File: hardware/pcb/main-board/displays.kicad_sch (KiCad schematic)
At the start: 1 part, among them J601 DISP_PCB x40 FPC

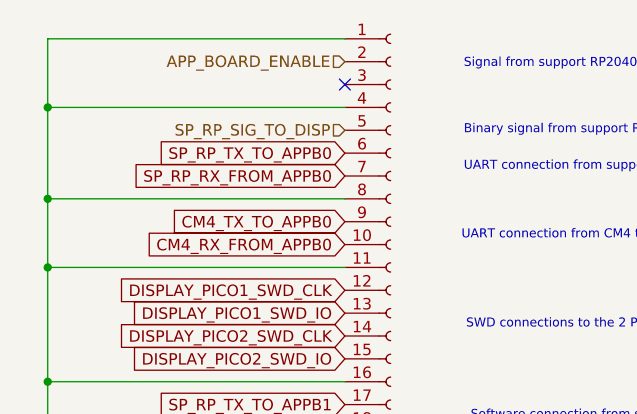
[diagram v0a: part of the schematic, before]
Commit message: more renaming and tidying up of internal interfaces
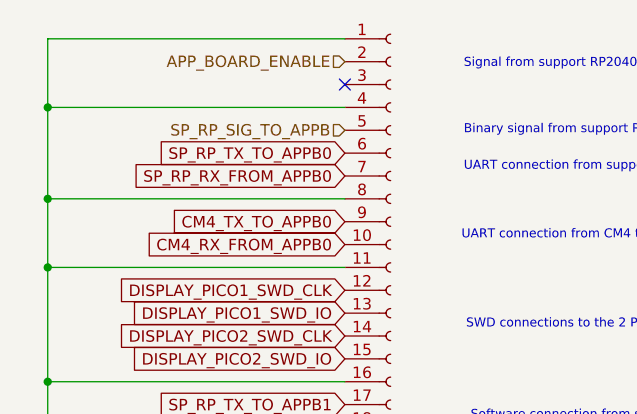
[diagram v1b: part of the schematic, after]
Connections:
- net SP_RP_SIG_TO_DISP renamed SP_RP_SIG_TO_APPB
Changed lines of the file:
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@@
 		)
 	)
-	(hierarchical_label "SP_RP_SIG_TO_DISP"
+	(hierarchical_label "SP_RP_SIG_TO_APPB"
 		(shape input)
 		(at 58.42 33.02 180)

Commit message: tidy the keyboard comms
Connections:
- net KB_TX_TO_APPB0: now reaches J601.19 (Pin_19)
- net KB_RX_FROM_APPB0: now reaches J601.20 (Pin_20)
- net KB_TX_TO_APPB1: now reaches J601.21 (Pin_21)
- net KB_RX_FROM_APPB1: now reaches J601.22 (Pin_22)
- net DISPLAY_PICO1_SWD_CLK renamed APPB_PICO0_SWD_CLK
- net DISPLAY_PICO1_SWD_IO renamed APPB_PICO0_SWD_IO
- net DISPLAY_PICO2_SWD_CLK renamed APPB_PICO1_SWD_CLK
- net DISPLAY_PICO2_SWD_IO renamed APPB_PICO1_SWD_IO
- no-connect marks 15 -> 11
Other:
- note added: "Software connection from keyboard RP to application board Pico1"
- note added: "UART connection from keyboard RP to application board Pico0"
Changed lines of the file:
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@@
-	)
-	(no_connect
-		(at 58.42 68.58)
 	)
 	(no_connect
@@
 	)
 	(no_connect
-		(at 58.42 76.2)
-	)
-	(no_connect
-		(at 58.42 71.12)
-	)
-	(no_connect
 		(at 58.42 101.6)
 	)
@@
 		(at 58.42 99.06)
 	)
-	(no_connect
-		(at 58.42 73.66)
-	)
 	(wire
 		(pts
@@
 		)
 	)
+	(text "Software connection from keyboard RP to application board Pico1"
+		(exclude_from_sim no)
+		(at 72.39 74.93 0)
+		(effects
+			(font
+				(size 1 1)
+			)
+			(justify left)
+		)
+	)
 	(text "Software connection from support RP2040 to application board Pico1"
 		(exclude_from_sim no)
@@
 		)
 	)
+	(text "UART connection from keyboard RP to application board Pico0"
+		(exclude_from_sim no)
+		(at 72.39 69.85 0)
+		(effects
+			(font
+				(size 1 1)
+			)
+			(justify left)
+		)
+	)
 	(text "UART connection from CM4 to application board Pico0"
 		(exclude_from_sim no)
@@
 		)
 	)
-	(global_label "DISPLAY_PICO2_SWD_IO"
+	(global_label "APPB_PICO1_SWD_IO"
 		(shape input)
 		(at 58.42 58.42 180)
@@
 		)
 		(property "Intersheetrefs" "${INTERSHEET_REFS}"
-			(at 34.0756 58.42 0)
+			(at 36.7366 58.42 0)
 			(effects
 				(font
@@
 		)
 	)
-	(global_label "DISPLAY_PICO2_SWD_CLK"
+	(global_label "APPB_PICO1_SWD_CLK"
 		(shape input)
 		(at 58.42 55.88 180)
@@
 		)
 		(property "Intersheetrefs" "${INTERSHEET_REFS}"
-			(at 32.4428 55.88 0)
+			(at 35.1038 55.88 0)
 			(effects
 				(font
@@
 		)
 	)
-	(global_label "DISPLAY_PICO1_SWD_CLK"
+	(global_label "APPB_PICO0_SWD_CLK"
 		(shape input)
 		(at 58.42 50.8 180)
@@
 		)
 		(property "Intersheetrefs" "${INTERSHEET_REFS}"
-			(at 32.4428 50.8 0)
+			(at 35.1038 50.8 0)
 			(effects
 				(font
@@
 		)
 	)
-	(global_label "DISPLAY_PICO1_SWD_IO"
+	(global_label "KB_TX_TO_APPB1"
+		(shape input)
+		(at 58.42 73.66 180)
+		(fields_autoplaced yes)
+		(effects
+			(font
+				(size 1.27 1.27)
+			)
+			(justify right)
+		)
+		(property "Intersheetrefs" "${INTERSHEET_REFS}"
+			(at 40.0629 73.66 0)
+			(effects
+				(font
+					(size 1.27 1.27)
+				)
+				(justify right)
+				(hide yes)
+			)
+		)
+	)
+	(global_label "KB_RX_FROM_APPB0"
+		(shape input)
+		(at 58.42 71.12 180)
+		(fields_autoplaced yes)
+		(effects
+			(font
+				(size 1.27 1.27)
+			)
+			(justify right)
+		)
+		(property "Intersheetrefs" "${INTERSHEET_REFS}"
+			(at 36.9181 71.12 0)
+			(effects
+				(font
+					(size 1.27 1.27)
+				)
+				(justify right)
+				(hide yes)
+			)
+		)
+	)
+	(global_label "KB_TX_TO_APPB0"
+		(shape input)
+		(at 58.42 68.58 180)
+		(fields_autoplaced yes)
+		(effects
+			(font
+				(size 1.27 1.27)
+			)
+			(justify right)
+		)
+		(property "Intersheetrefs" "${INTERSHEET_REFS}"
+			(at 40.0629 68.58 0)
+			(effects
+				(font
+					(size 1.27 1.27)
+				)
+				(justify right)
+				(hide yes)
+			)
+		)
+	)
+	(global_label "APPB_PICO0_SWD_IO"
 		(shape input)
 		(at 58.42 53.34 180)
@@
 		)
 		(property "Intersheetrefs" "${INTERSHEET_REFS}"
-			(at 34.0756 53.34 0)
+			(at 36.7366 53.34 0)
 			(effects
 				(font
@@
 			(effects
 				(font
+					(size 1.27 1.27)
+				)
+				(justify right)
+				(hide yes)
+			)
+		)
+	)
+	(global_label "KB_RX_FROM_APPB1"
+		(shape input)
+		(at 58.42 76.2 180)
+		(fields_autoplaced yes)
+		(effects
+			(font
+				(size 1.27 1.27)
+			)
+			(justify right)
+		)
+		(property "Intersheetrefs" "${INTERSHEET_REFS}"
+			(at 36.9181 76.2 0)
+			(effects
+				(font

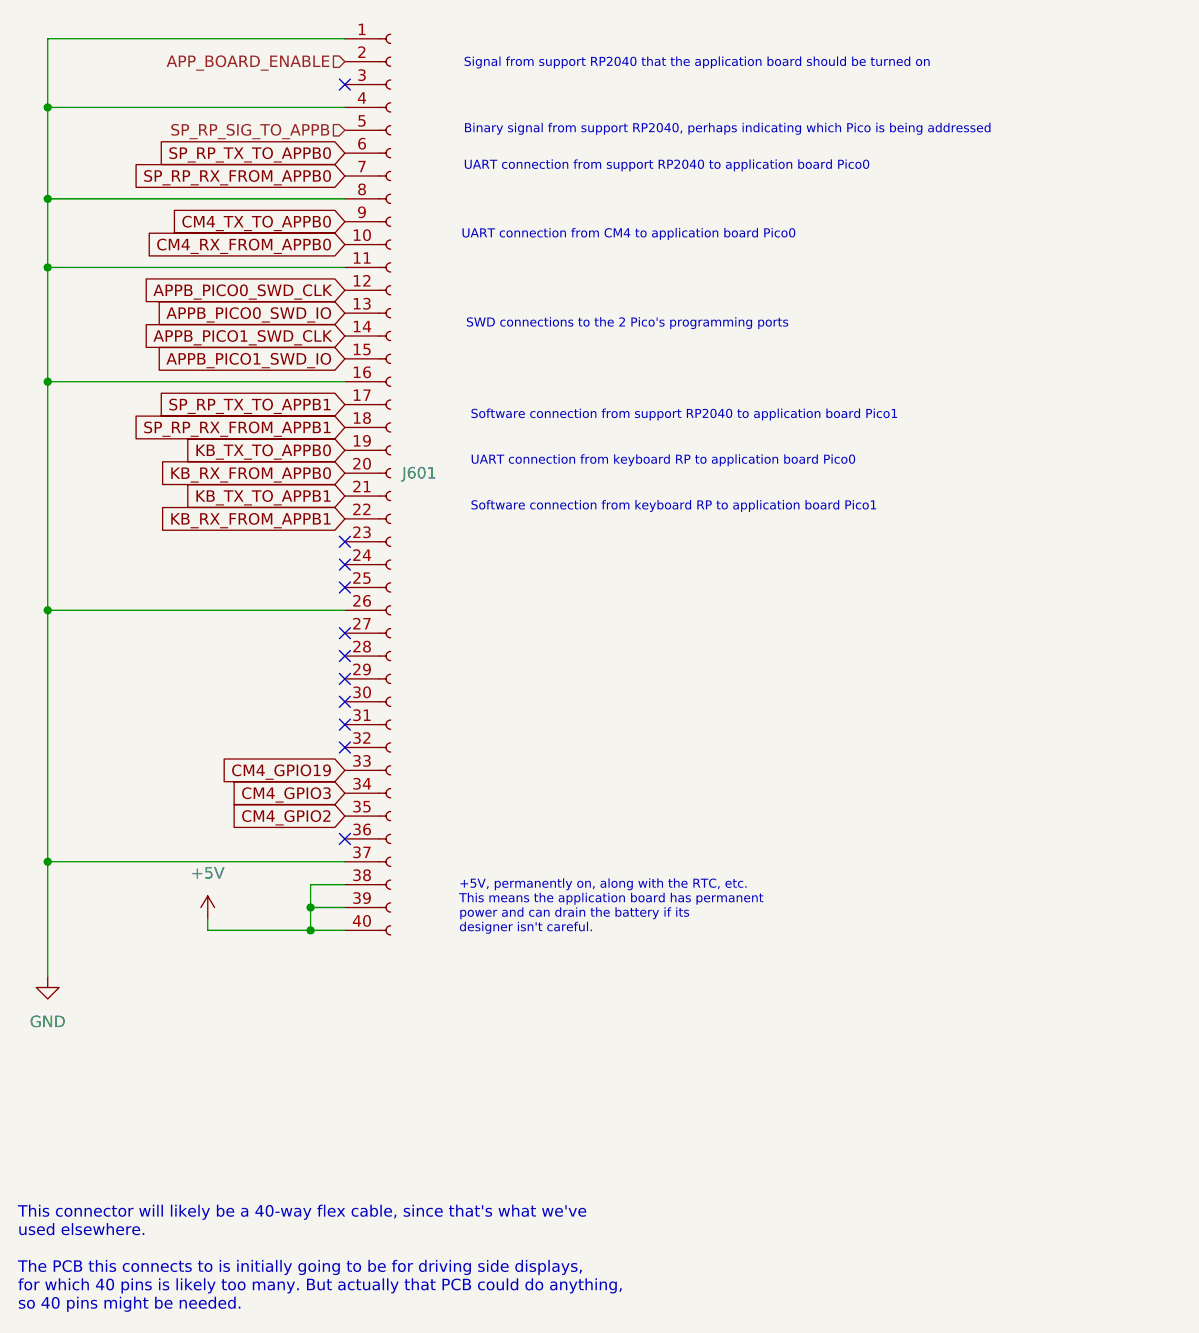
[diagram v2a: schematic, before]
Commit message: rename app board picos to 1 and 2, to match the application board schematics
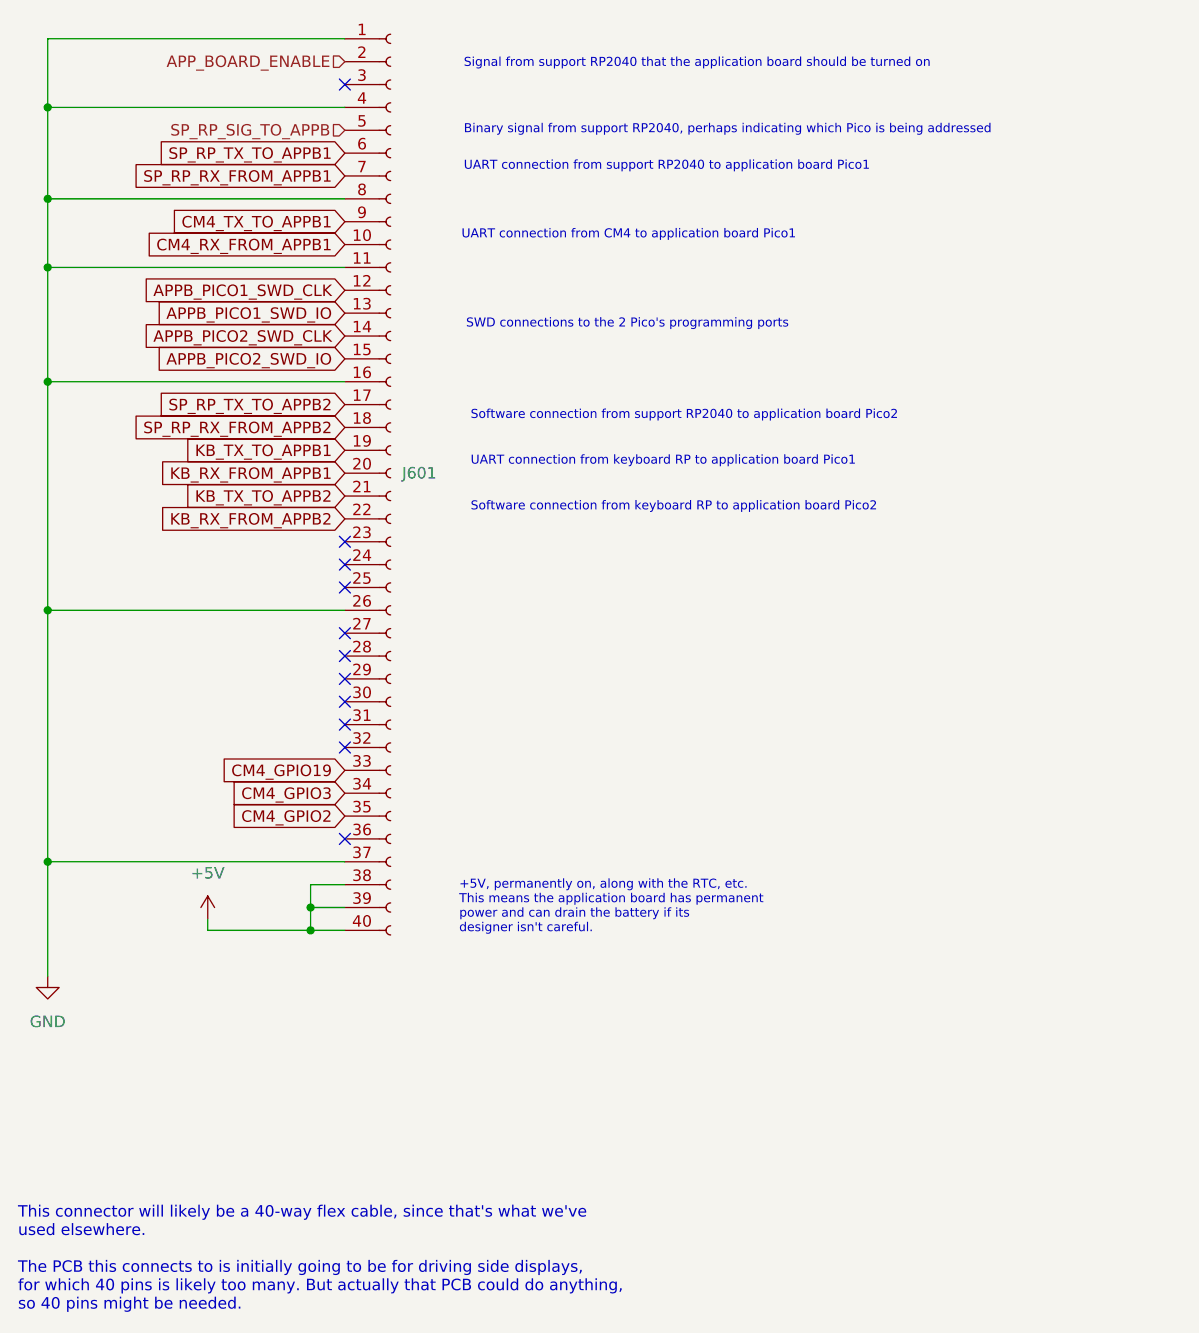
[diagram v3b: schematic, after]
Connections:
- net APPB_PICO0_SWD_CLK is gone; now on net APPB_PICO1_SWD_CLK: J601.12 (Pin_12)
- net APPB_PICO0_SWD_IO is gone; now on net APPB_PICO1_SWD_IO: J601.13 (Pin_13)
- net KB_RX_FROM_APPB0 is gone; now on net KB_RX_FROM_APPB1: J601.20 (Pin_20)
- net KB_TX_TO_APPB0 is gone; now on net KB_TX_TO_APPB1: J601.19 (Pin_19)
- net SP_RP_RX_FROM_APPB0 is gone; now on net SP_RP_RX_FROM_APPB1: J601.7 (Pin_7)
- net SP_RP_TX_TO_APPB0 is gone; now on net SP_RP_TX_TO_APPB1: J601.6 (Pin_6)
- net APPB_PICO1_SWD_CLK: no longer J601.14 (Pin_14)
- net APPB_PICO1_SWD_IO: no longer J601.15 (Pin_15)
- net KB_RX_FROM_APPB1: no longer J601.22 (Pin_22)
- net KB_TX_TO_APPB1: no longer J601.21 (Pin_21)
- net SP_RP_RX_FROM_APPB1: no longer J601.18 (Pin_18)
- net SP_RP_TX_TO_APPB1: no longer J601.17 (Pin_17)
- net CM4_RX_FROM_APPB0 renamed CM4_RX_FROM_APPB1
- net CM4_TX_TO_APPB0 renamed CM4_TX_TO_APPB1
- new net APPB_PICO2_SWD_CLK: J601.14 (Pin_14)
- new net APPB_PICO2_SWD_IO: J601.15 (Pin_15)
- new net KB_RX_FROM_APPB2: J601.22 (Pin_22)
- new net KB_TX_TO_APPB2: J601.21 (Pin_21)
- new net SP_RP_RX_FROM_APPB2: J601.18 (Pin_18)
- new net SP_RP_TX_TO_APPB2: J601.17 (Pin_17)
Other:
- note added: "Software connection from keyboard RP to application board Pico2"
- note added: "Software connection from support RP2040 to application board Pico2"
- note added: "UART connection from CM4 to application board Pico1"
- note added: "UART connection from keyboard RP to application board Pico1"
- note added: "UART connection from support RP2040 to application board Pico1"
- note removed: "Software connection from keyboard RP to application board Pico1"
- note removed: "Software connection from support RP2040 to application board Pico1"
- note removed: "UART connection from CM4 to application board Pico0"
- note removed: "UART connection from keyboard RP to application board Pico0"
- note removed: "UART connection from support RP2040 to application board Pico0"

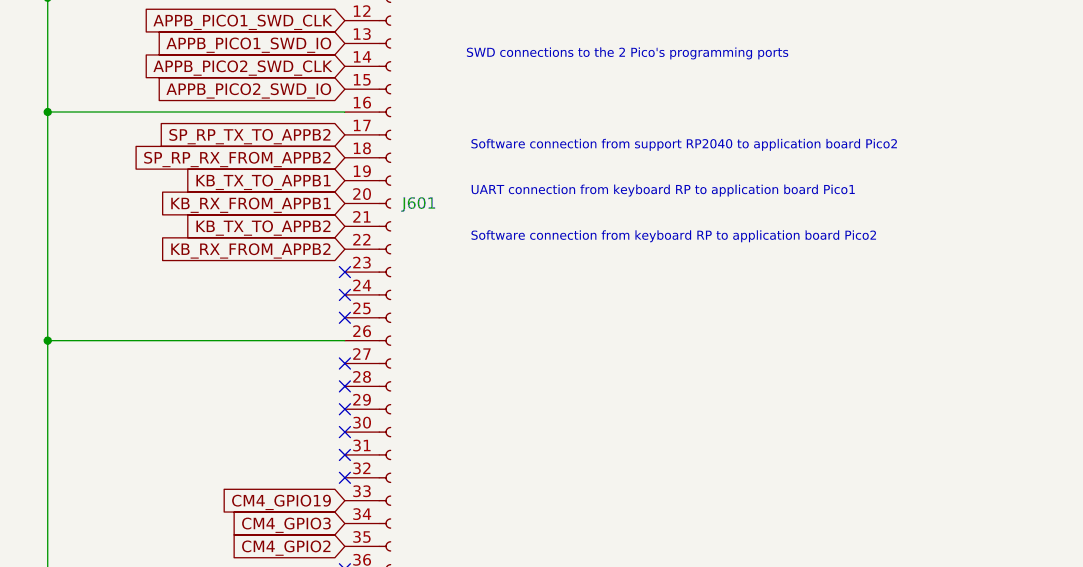
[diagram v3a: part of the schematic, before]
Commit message: move an SWD GPIO freeing up UART4 on the CM4. use that for talking to the appb Pico2
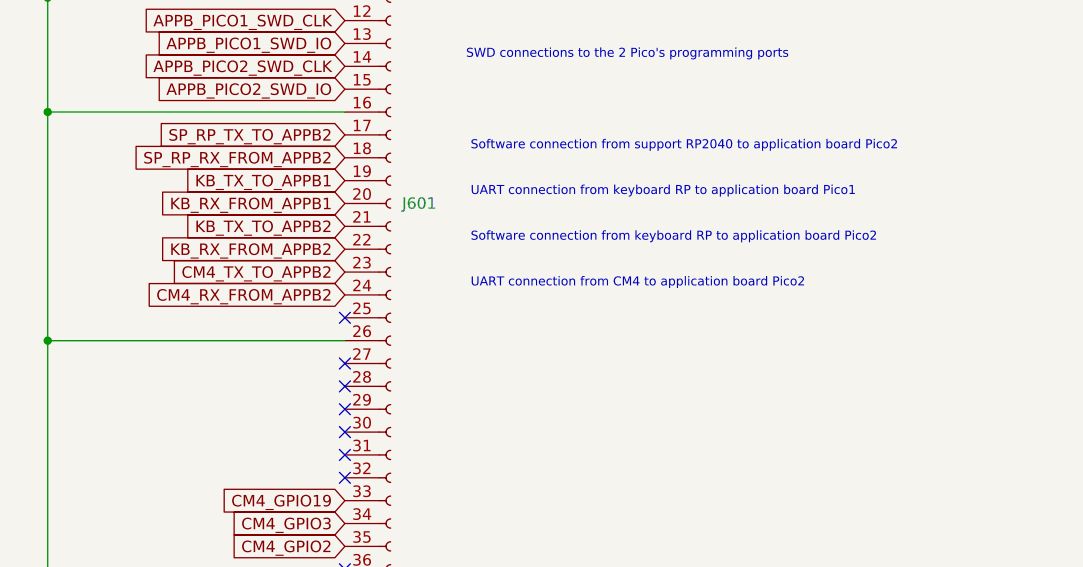
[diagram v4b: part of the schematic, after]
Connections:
- net CM4_TX_TO_APPB2: now reaches J601.23 (Pin_23)
- net CM4_RX_FROM_APPB2: now reaches J601.24 (Pin_24)
- no-connect marks 11 -> 9
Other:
- note added: "UART connection from CM4 to application board Pico2"
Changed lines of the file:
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@@
-	)
-	(no_connect
-		(at 58.42 81.28)
 	)
 	(no_connect
@@
 	)
 	(no_connect
-		(at 58.42 78.74)
-	)
-	(no_connect
 		(at 58.42 96.52)
 	)
@@
 		)
 	)
+	(text "UART connection from CM4 to application board Pico2"
+		(exclude_from_sim no)
+		(at 72.39 80.01 0)
+		(effects
+			(font
+				(size 1 1)
+			)
+			(justify left)
+		)
+	)
 	(global_label "APPB_PICO2_SWD_IO"
 		(shape input)
@@
 		)
 	)
+	(global_label "CM4_RX_FROM_APPB2"
+		(shape input)
+		(at 58.42 81.28 180)
+		(fields_autoplaced yes)
+		(effects
+			(font
+				(size 1.27 1.27)
+			)
+			(justify right)
+		)
+		(property "Intersheetrefs" "${INTERSHEET_REFS}"
+			(at 35.5272 81.28 0)
+			(effects
+				(font
+					(size 1.27 1.27)
+				)
+				(justify right)
+				(hide yes)
+			)
+		)
+	)
 	(global_label "CM4_GPIO3"
 		(shape input)
@@
 			(effects
 				(font
+					(size 1.27 1.27)
+				)
+				(justify right)
+				(hide yes)
+			)
+		)
+	)
+	(global_label "CM4_TX_TO_APPB2"
+		(shape input)
+		(at 58.42 78.74 180)
+		(fields_autoplaced yes)
+		(effects
+			(font
+				(size 1.27 1.27)
+			)
+			(justify right)
+		)
+		(property "Intersheetrefs" "${INTERSHEET_REFS}"
+			(at 38.672 78.74 0)
+			(effects
+				(font
